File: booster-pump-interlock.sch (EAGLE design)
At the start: 17 parts, among them IC1 OPA743, IC2 OPA743, IC3 4044D, IC4 OPA743, IC5 OPA743

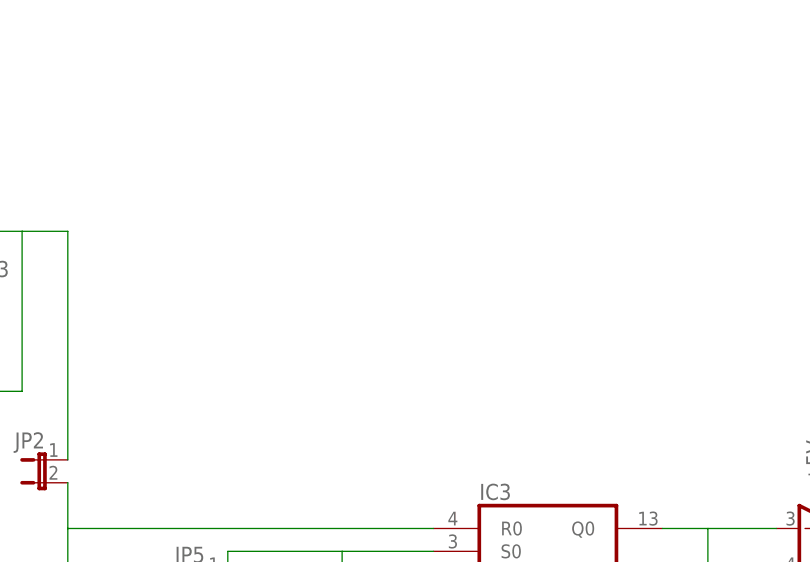
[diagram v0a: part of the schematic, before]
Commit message: added QR code & tag.
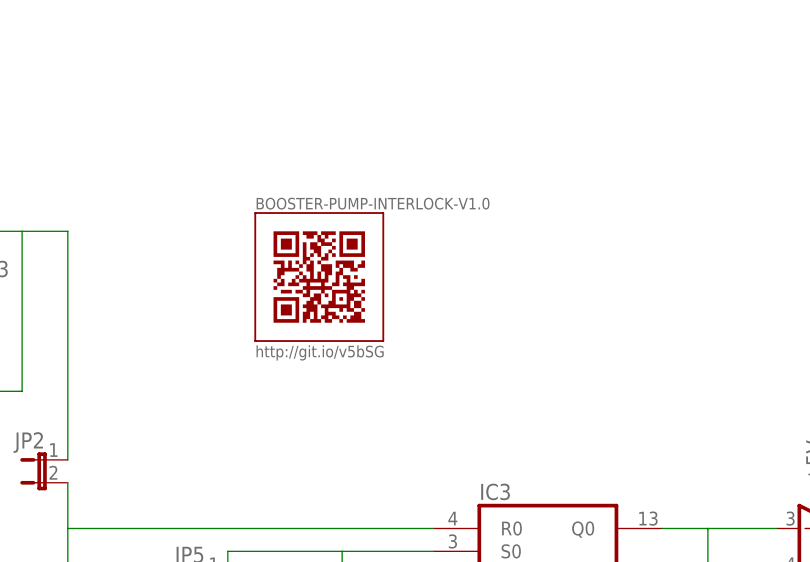
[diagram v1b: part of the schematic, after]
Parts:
- added BOOSTER-PUMP-INTERLOCK-V1.0: QR-HTTP://GIT.IO/V5BSG-WIRE, QR-git.io-v5bSG:QR-HTTP://GIT.IO/V5BSG-WIRE
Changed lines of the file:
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@@
 <part name="GND11" library="supply1" deviceset="GND" device=""/>
 <part name="GND12" library="supply1" deviceset="GND" device=""/>
+<part name="BOOSTER-PUMP-INTERLOCK-V1.0" library="QR-git.io-v5bSG" deviceset="QR-HTTP://GIT.IO/V5BSG" device="-WIRE"/>
 </parts>
 <sheets>
@@
 <instance part="GND11" gate="1" x="106.68" y="7.62"/>
 <instance part="GND12" gate="1" x="185.42" y="66.04"/>
+<instance part="BOOSTER-PUMP-INTERLOCK-V1.0" gate="G$1" x="83.82" y="101.6"/>
 </instances>
 <busses>

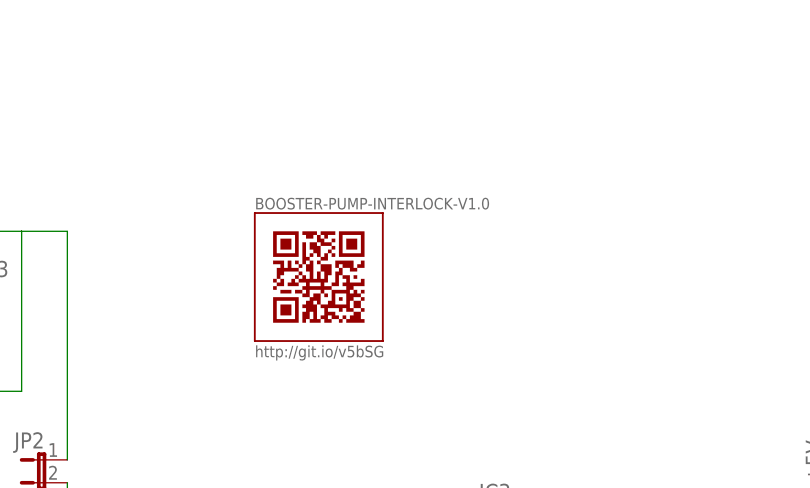
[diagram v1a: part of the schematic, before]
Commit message: added QR code & tag.
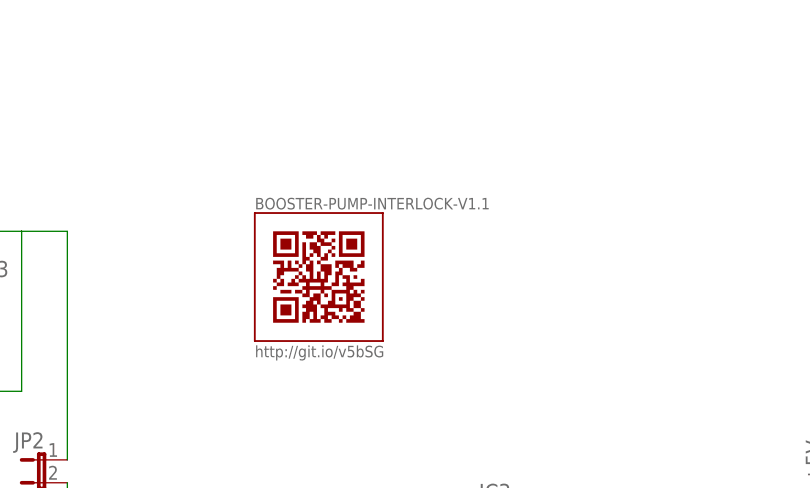
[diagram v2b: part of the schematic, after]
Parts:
- renumbered BOOSTER-PUMP-INTERLOCK-V1.0 to BOOSTER-PUMP-INTERLOCK-V1.1
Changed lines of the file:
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@@
 <setting verticaltext="up"/>
 </settings>
-<grid distance="0.1" unitdist="inch" unit="inch" style="lines" multiple="1" display="yes" altdistance="0.01" altunitdist="inch" altunit="inch"/>
+<grid distance="0.1" unitdist="inch" unit="inch" style="lines" multiple="1" display="no" altdistance="0.01" altunitdist="inch" altunit="inch"/>
 <layers>
 <layer number="1" name="Top" color="4" fill="1" visible="no" active="no"/>
@@
 <part name="GND11" library="supply1" deviceset="GND" device=""/>
 <part name="GND12" library="supply1" deviceset="GND" device=""/>
-<part name="BOOSTER-PUMP-INTERLOCK-V1.0" library="QR-git.io-v5bSG" deviceset="QR-HTTP://GIT.IO/V5BSG" device="-WIRE"/>
+<part name="BOOSTER-PUMP-INTERLOCK-V1.1" library="QR-git.io-v5bSG" deviceset="QR-HTTP://GIT.IO/V5BSG" device="-WIRE"/>
 </parts>
 <sheets>
@@
 <instance part="GND11" gate="1" x="106.68" y="7.62"/>
 <instance part="GND12" gate="1" x="185.42" y="66.04"/>
-<instance part="BOOSTER-PUMP-INTERLOCK-V1.0" gate="G$1" x="83.82" y="101.6"/>
+<instance part="BOOSTER-PUMP-INTERLOCK-V1.1" gate="G$1" x="83.82" y="101.6"/>
 </instances>
 <busses>

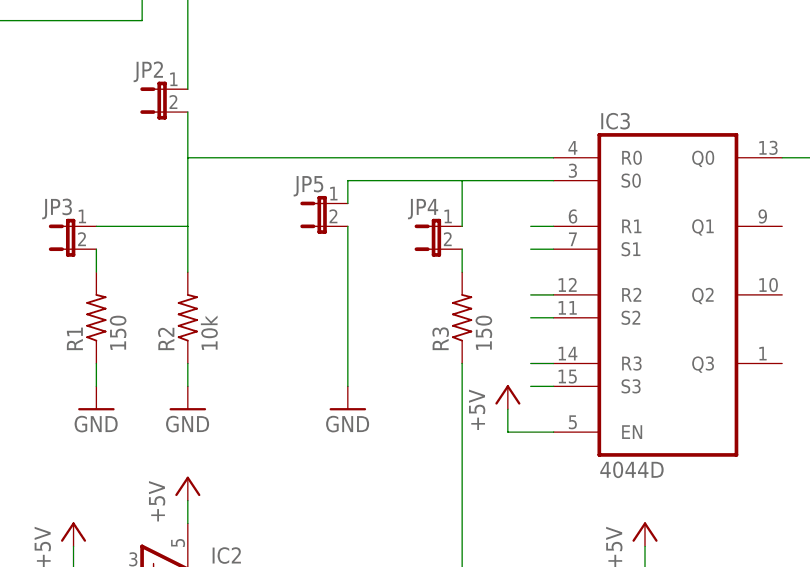
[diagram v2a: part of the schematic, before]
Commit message: Added pulldown resistor to fix tripping issue due to charge buildup on pulldown diode
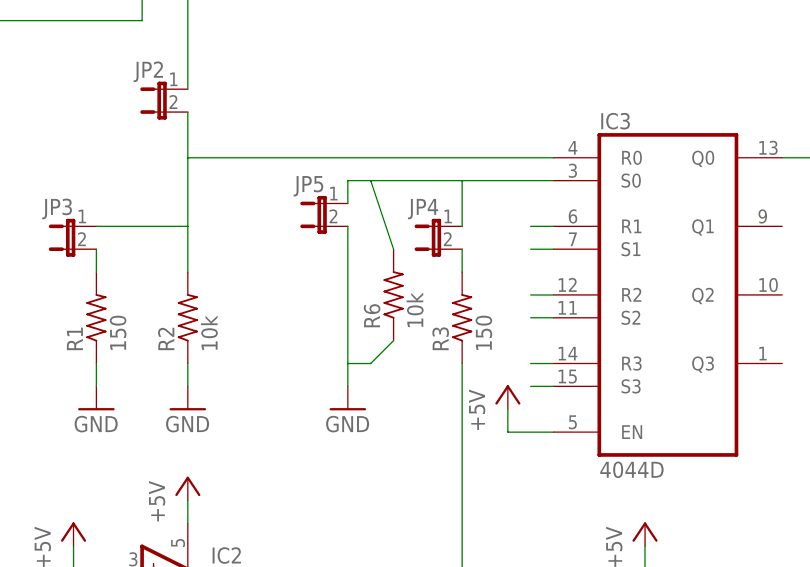
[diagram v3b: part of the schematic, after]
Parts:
- added R6: 10k, rcl:R-US_M1206
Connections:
- net GND: now also R6.1
- net S0: now also R6.2
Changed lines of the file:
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@@
 <?xml version="1.0" encoding="utf-8"?>
 <!DOCTYPE eagle SYSTEM "eagle.dtd">
-<eagle version="7.7.0">
+<eagle version="9.0.1">
 <drawing>
 <settings>
 <setting alwaysvectorfont="no"/>
+<setting keepoldvectorfont="yes"/>
 <setting verticaltext="up"/>
 </settings>
-<grid distance="0.1" unitdist="inch" unit="inch" style="lines" multiple="1" display="no" altdistance="0.01" altunitdist="inch" altunit="inch"/>
+<grid distance="0.1" unitdist="inch" unit="inch" style="lines" multiple="1" display="yes" altdistance="0.01" altunitdist="inch" altunit="inch"/>
 <layers>
 <layer number="1" name="Top" color="4" fill="1" visible="no" active="no"/>
@@
 <part name="GND12" library="supply1" deviceset="GND" device=""/>
 <part name="BOOSTER-PUMP-INTERLOCK-V1.1" library="QR-git.io-v5bSG" deviceset="QR-HTTP://GIT.IO/V5BSG" device="-WIRE"/>
+<part name="R6" library="rcl" deviceset="R-US_" device="M1206" value="10k"/>
 </parts>
 <sheets>
@@
 <instance part="GND12" gate="1" x="185.42" y="66.04"/>
 <instance part="BOOSTER-PUMP-INTERLOCK-V1.1" gate="G$1" x="83.82" y="101.6"/>
+<instance part="R6" gate="G$1" x="78.74" y="58.42" rot="R90"/>
 </instances>
 <busses>
@@
 <pinref part="JP5" gate="A" pin="2"/>
 <pinref part="GND6" gate="1" pin="GND"/>
-<wire x1="73.66" y1="66.04" x2="73.66" y2="48.26" width="0.1524" layer="91"/>
+<wire x1="73.66" y1="66.04" x2="73.66" y2="50.8" width="0.1524" layer="91"/>
+<wire x1="73.66" y1="50.8" x2="73.66" y2="48.26" width="0.1524" layer="91"/>
+<wire x1="78.74" y1="53.34" x2="76.2" y2="50.8" width="0.1524" layer="91"/>
+<wire x1="76.2" y1="50.8" x2="73.66" y2="50.8" width="0.1524" layer="91"/>
+<pinref part="R6" gate="G$1" pin="1"/>
 </segment>
 <segment>
@@
 <wire x1="86.36" y1="66.04" x2="86.36" y2="71.12" width="0.1524" layer="91"/>
 <pinref part="JP5" gate="A" pin="1"/>
-<wire x1="86.36" y1="71.12" x2="73.66" y2="71.12" width="0.1524" layer="91"/>
+<wire x1="86.36" y1="71.12" x2="76.2" y2="71.12" width="0.1524" layer="91"/>
+<wire x1="76.2" y1="71.12" x2="73.66" y2="71.12" width="0.1524" layer="91"/>
 <wire x1="73.66" y1="71.12" x2="73.66" y2="68.58" width="0.1524" layer="91"/>
-</segment>
-</net>
+<wire x1="78.74" y1="63.5" x2="76.2" y2="71.12" width="0.1524" layer="91"/>
+<pinref part="R6" gate="G$1" pin="2"/>
+</segment>
+</net>
